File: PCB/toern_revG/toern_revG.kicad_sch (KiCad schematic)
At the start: 96 parts, among them IC1 BQ24075TRGTR, J1 AudioJack3_Switch, J10 Conn_01x02, J11 Conn_01x05, J11.5 Conn_01x05, J12 Conn_01x05, J13 Conn_01x05, J14 Conn_01x05, J15 Conn_01x05, J16 BATTERY, J17 AudioJack3_Ground, J3 AudioJack3_Ground, J4 USB_C_Receptacle_USB2.0, J5 AudioJack3_Switch, J6 AudioJack3_Switch, J7 AudioJack3_Switch, J8 Micro_SD_Card, J9 Conn_01x03, U1 SPX3819M5-L-3-3, U10 01x05 Connector_PinSocket_2.5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, U11 01x05 Connector_PinSocket_2.5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, U12 01x05 Connector_PinSocket_2.5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, U13 PAM8403D, U2 SPX3819M5-L-1-8, U3 SGTL5000XNBA3, U4 TLP2361V4_E, U5 74LVC2G14, U6 Teensy4.1, U7 SPX3819M5-L-3-3, U9 01x05 Connector_PinSocket_2.5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

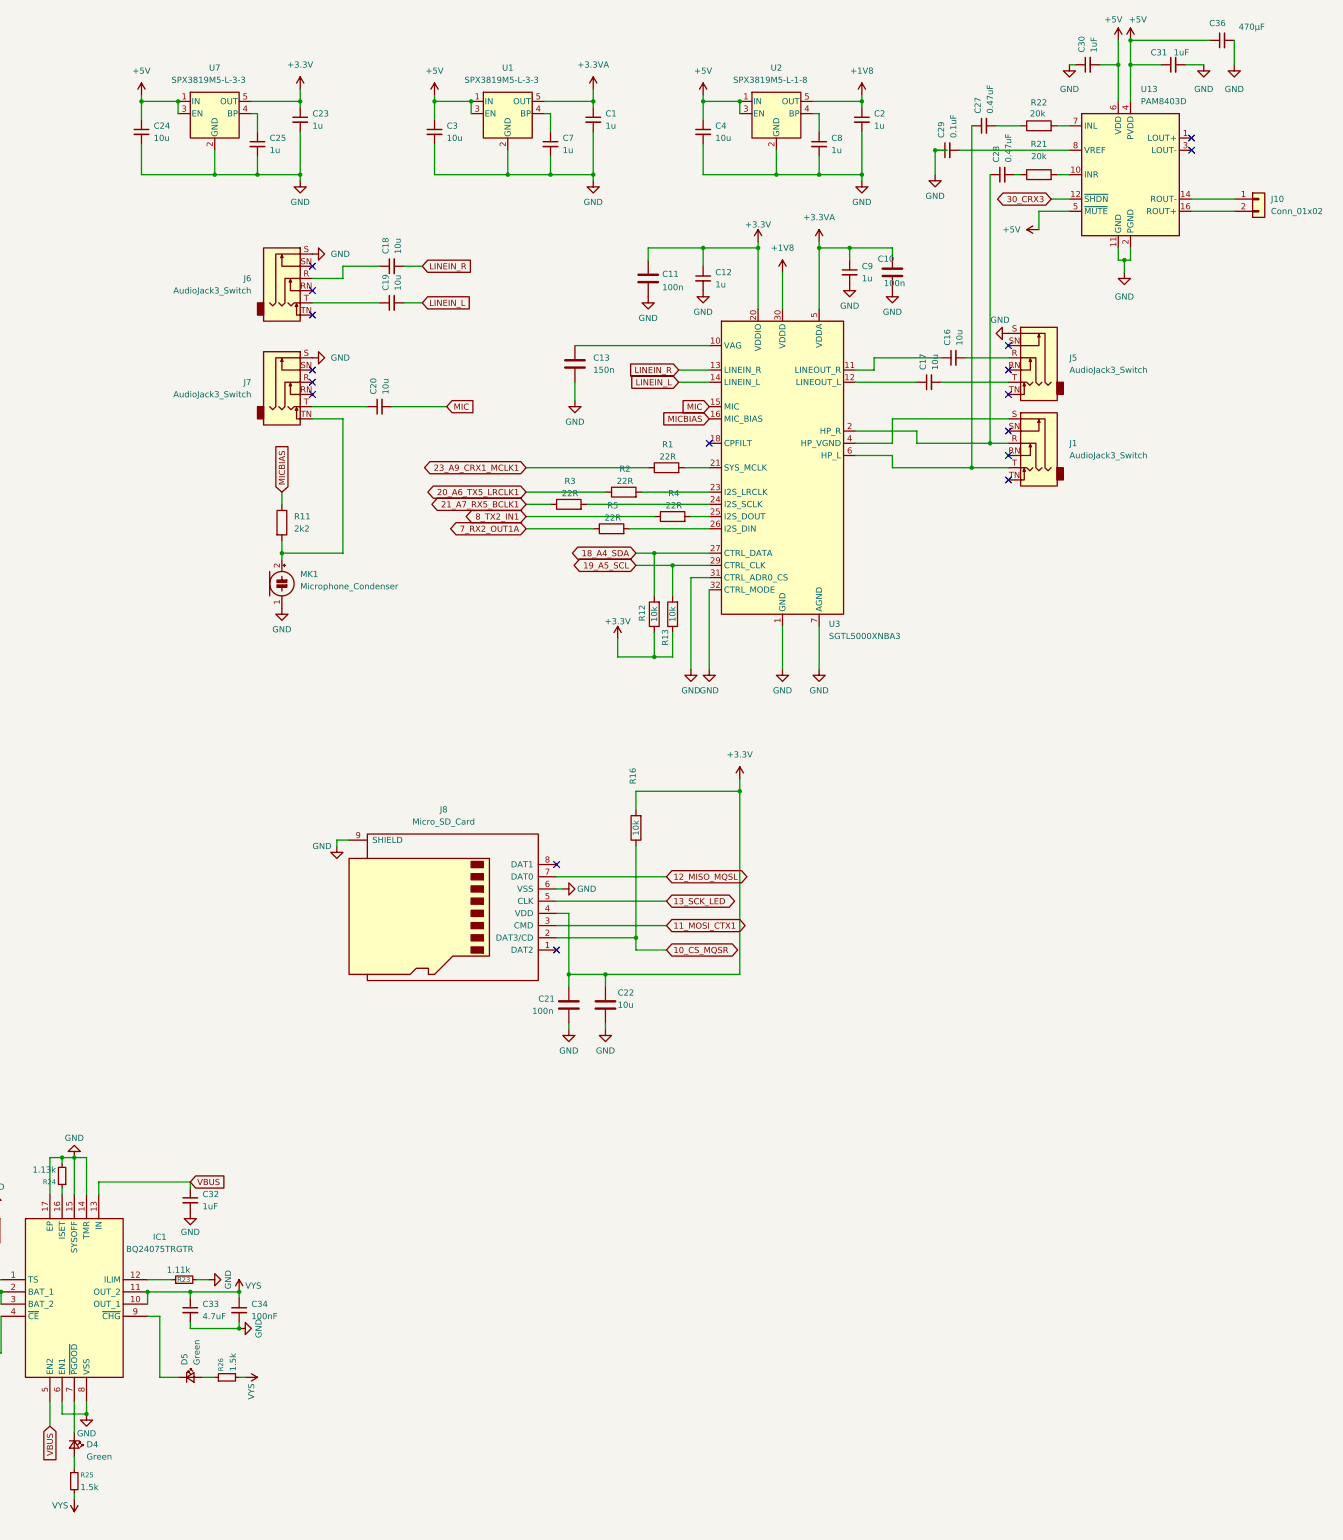
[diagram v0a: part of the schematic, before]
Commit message: fixes for HD Displays 32x16
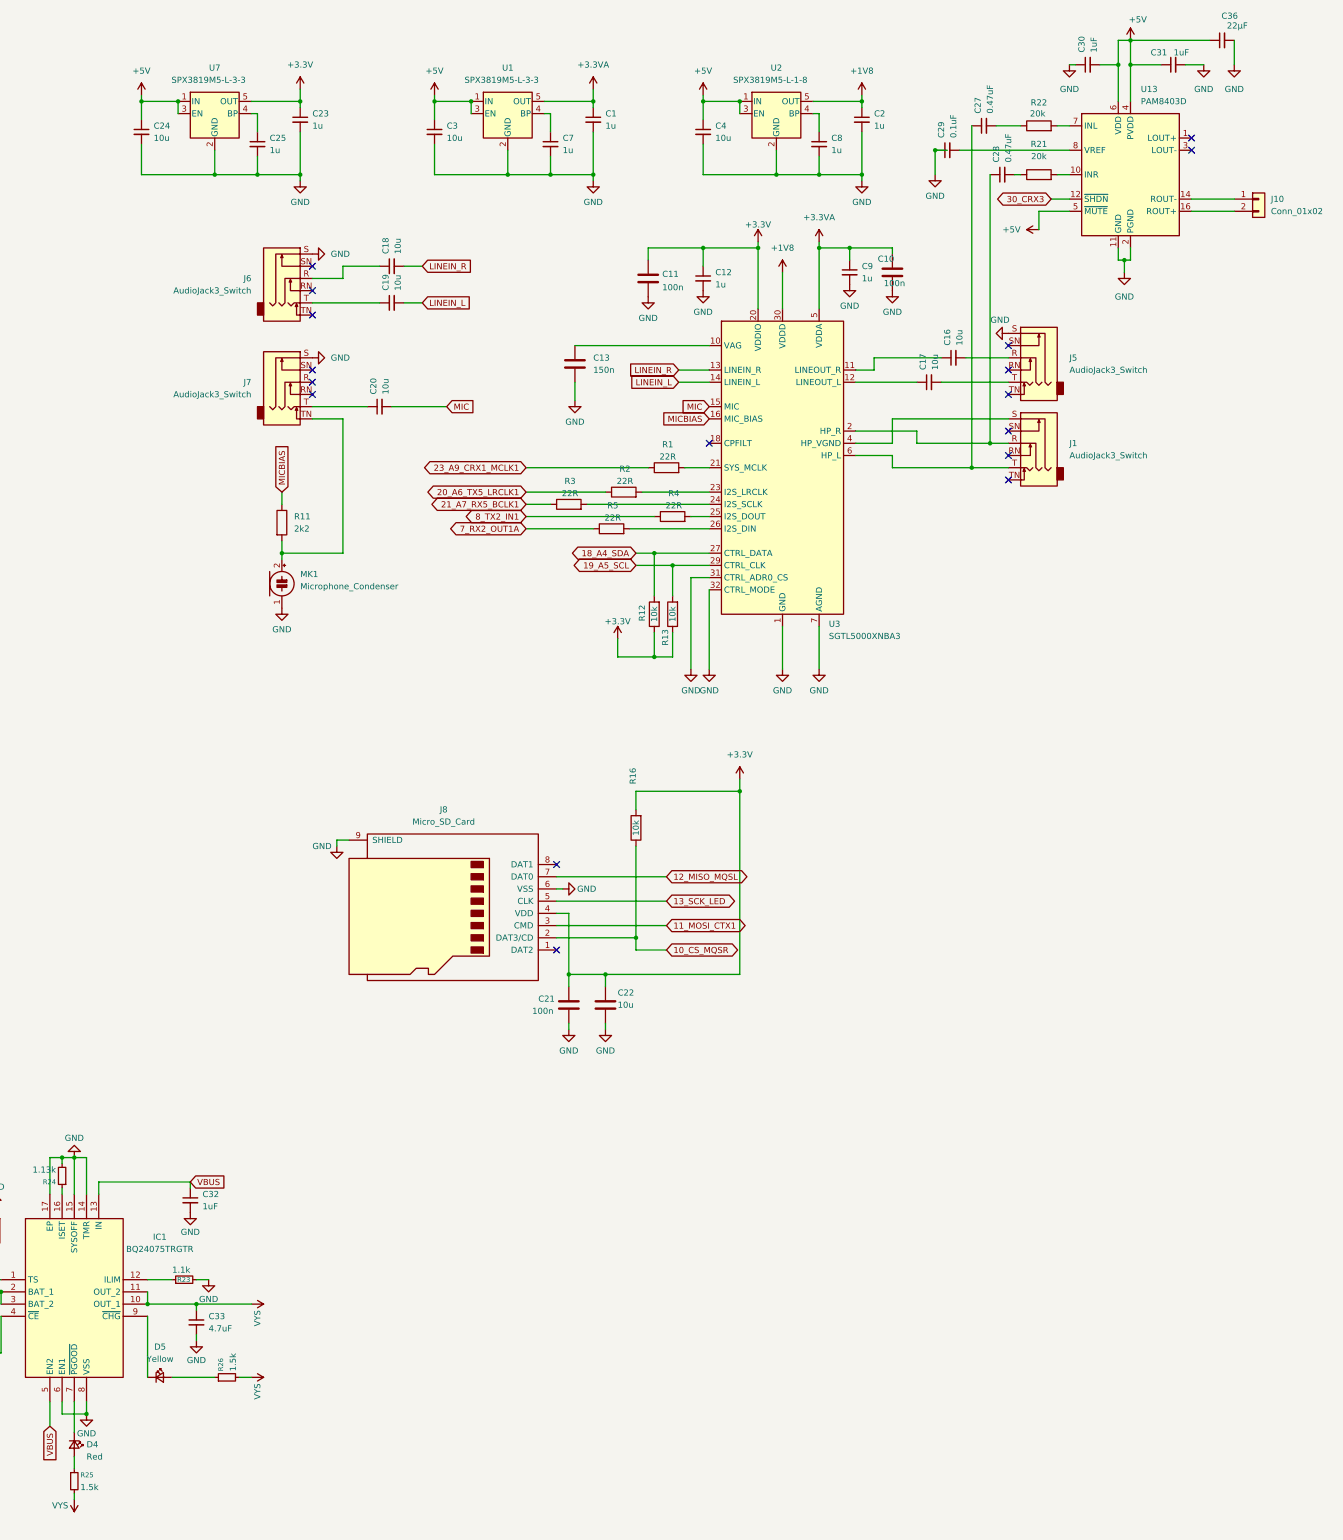
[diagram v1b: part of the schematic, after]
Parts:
- removed C34: 100nF, Capacitor_SMD:C_0402_1005Metric, symbol Device:C_Small
- C32: lcsc# (none) -> C15849
- C35: lscs# (none) -> C1705
- C36: value 470µF -> 22µF; lcsc# (none) -> C1859
- D4: value Green -> Red; lcsc# (none) -> C71911
- D5: value Green -> Yellow; lcsc# (none) -> C74342
- R14: lcsc# C98220 -> C25744
- R23: value 1.11k -> 1.1k; lcsc# (none) -> C25860
- R24: lcsc# (none) -> C67014
- R25, R26: lcsc# (none) -> C25867
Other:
- moved on the sheet: C33, D5

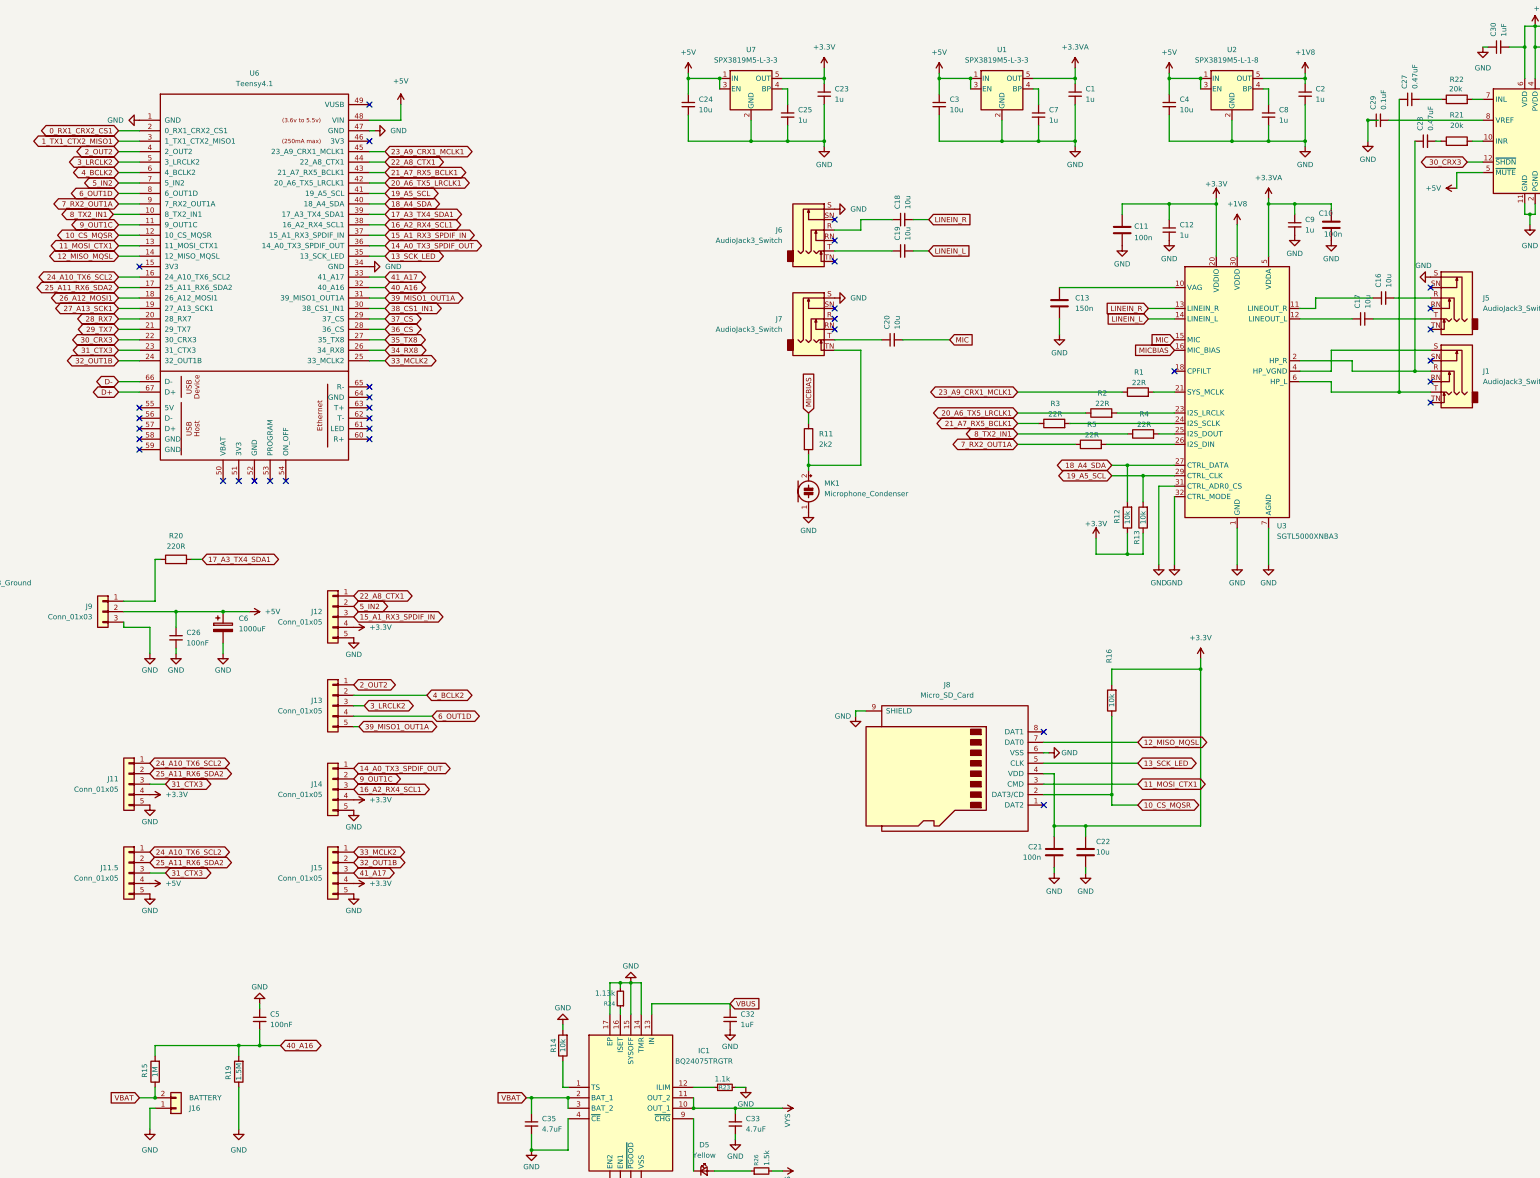
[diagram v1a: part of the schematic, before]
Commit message: extended reverb and muteAll fix for Draw==R
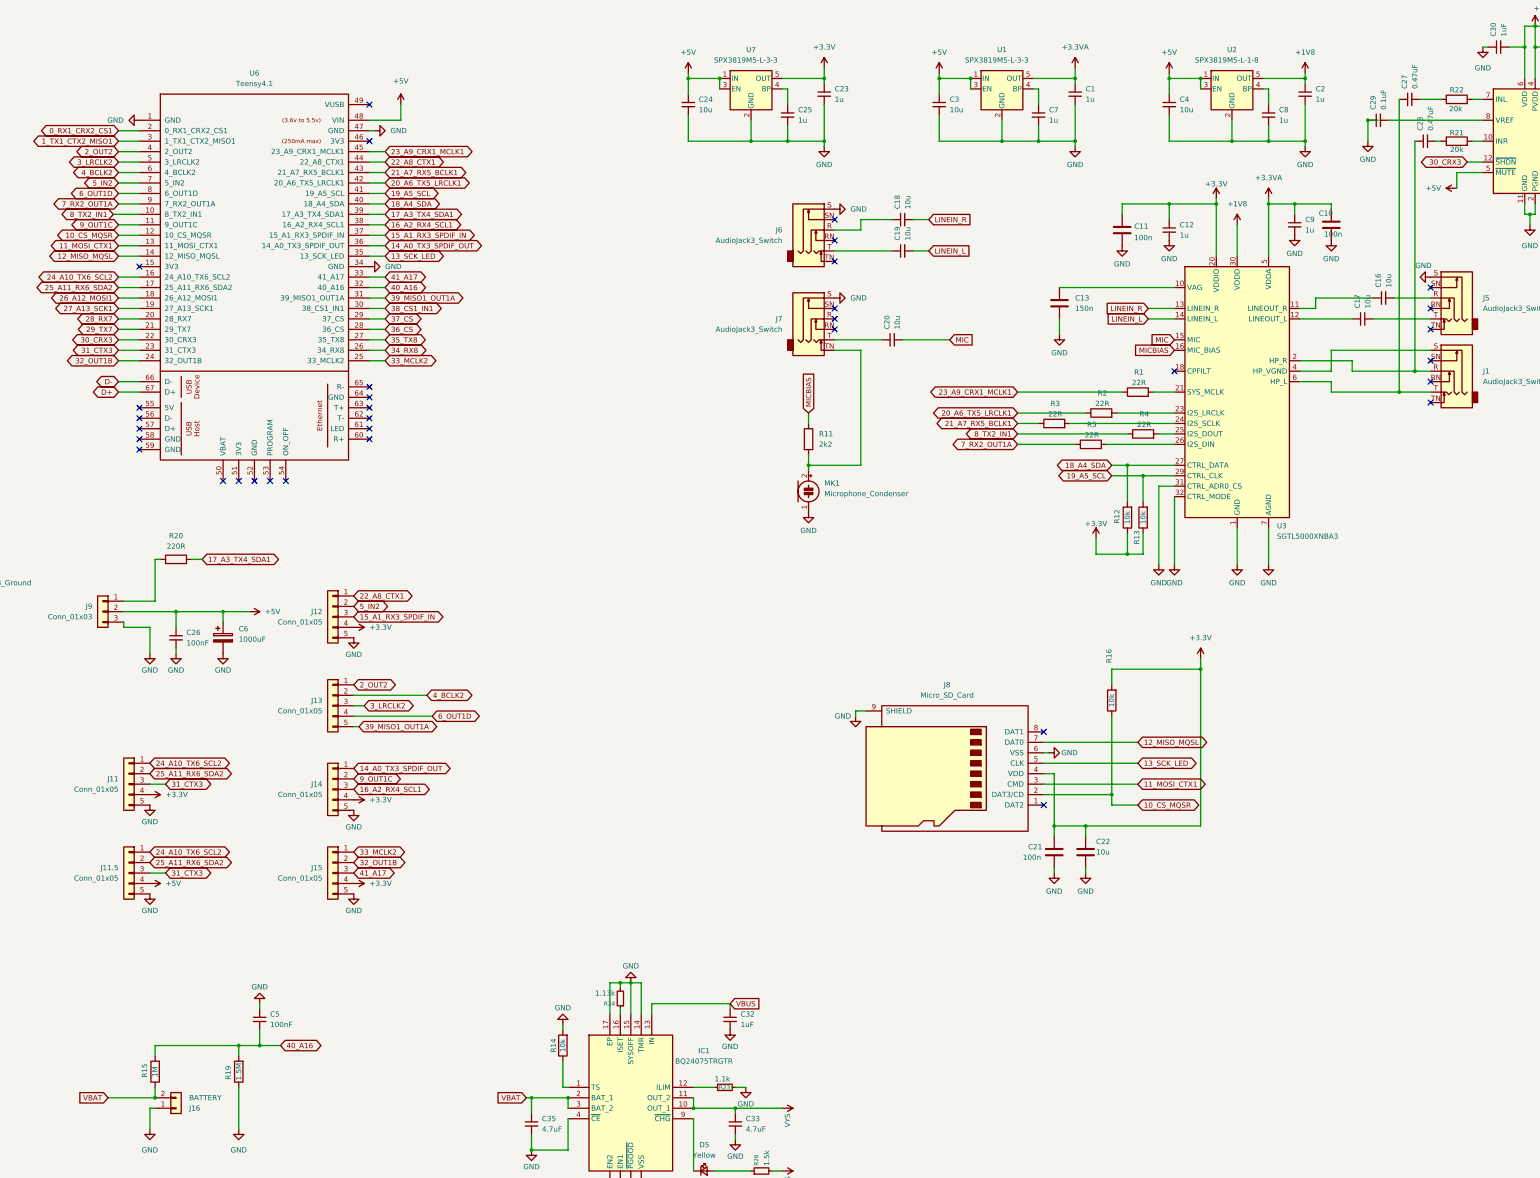
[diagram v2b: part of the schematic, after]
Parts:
- C26: lcsc# (none) -> C1525
- C35: lcsc# (none) -> C1705
- C6: lcsc# (none) -> C5686929
- IC1: lcsc# (none) -> C544783
- J17, J3: lcsc# (none) -> C4992548
- MK1: footprint Sensor_Audio:POM-2244P-C3310-2-R -> GMI6027P-2C38DB-RF75; lcsc# C3273559 -> C529951
- R21, R22: lcsc# (none) -> C4328; lcsnr# C4184 -> C4328
- S1: lcsc# (none) -> C3664594
- U13: lcsc# (none) -> C17337
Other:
- moved on the sheet: C6

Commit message: fixed PCB and shematics for RevG
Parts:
- added MountingHole1, MountingHole2, MountingHole3: MountingHole_2.2mm_M2, MountingHole:MountingHole_2.2mm_M2, symbol Mechanical:MountingHole
- C26: footprint Capacitor_SMD:C_0201_0603Metric -> Capacitor_SMD:C_0603_1608Metric; lcsc# C1525 -> C1590
- C29: value 0.1uF -> 100nF; lcsc# C1525 -> C1590
- C30, C31: lcsc# C1848 -> C15849
- C35: lscs# C1705 -> (none)
- C36: lcsc# C1859 -> C59461
- C5: footprint Capacitor_SMD:C_0402_1005Metric -> Capacitor_SMD:C_0603_1608Metric; LCSC (none) -> C1590; lcsc# C1525 -> C1590
- IC1: LCSC (none) -> C544783
- J16: value BATTERY -> Conn_01x02
- J17, J3: LCSC (none) -> C4992548
- MK1: footprint GMI6027P-2C38DB-RF75 -> Sensor_Audio:POM-2244P-C3310-2-R
- R11: value 2k2 -> 2.2k
- R12, R13, R16: lcsc# C98220 -> C25744
- R21, R22: LCSC (none) -> C4328; lcsnr# C4328 -> (none)
- S1: footprint EG2219 -> Button_Switch_THT:SW_E-Switch_EG2219_DPDT_Angled; LCSC (none) -> C3664594
- U13: LCSC (none) -> C17337
- U3: LCSC (none) -> C5196742; lcsc# C5196742 -> C5196742
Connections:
- net +5V: now also J9.3 (Pin_3); no longer J9.2 (Pin_2)
- net GND: now also J9.2 (Pin_2); no longer J9.3 (Pin_3)
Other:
- moved on the sheet: C26, C6, J9, R20

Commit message: fixed PCB and shematics for RevG 2
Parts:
- added J18, J19, J2, J20, J21, J22, J23, J24: Conn_01x05_Socket, Connector_PinSocket_2.54mm:PinSocket_1x05_P2.54mm_Vertical, symbol Connector:Conn_01x05_Socket
- U10, U11, U12, U9: now left out of the parts list
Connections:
- net +5V: now also J18.2 (Pin_2), J19.2 (Pin_2), J2.2 (Pin_2), J20.2 (Pin_2), J21.2 (Pin_2), J22.2 (Pin_2), J23.2 (Pin_2), J24.2 (Pin_2)
- net 18_A4_SDA: now also J18.3 (Pin_3), J19.3 (Pin_3), J2.3 (Pin_3), J20.3 (Pin_3), J21.3 (Pin_3), J22.3 (Pin_3), J23.3 (Pin_3), J24.3 (Pin_3)
- net 19_A5_SCL: now also J18.4 (Pin_4), J19.4 (Pin_4), J2.4 (Pin_4), J20.4 (Pin_4), J21.4 (Pin_4), J22.4 (Pin_4), J23.4 (Pin_4), J24.4 (Pin_4)
- net 27_A13_SCK1: now also J18.5 (Pin_5), J19.5 (Pin_5), J2.5 (Pin_5), J20.5 (Pin_5), J21.5 (Pin_5), J22.5 (Pin_5), J23.5 (Pin_5), J24.5 (Pin_5)
- net GND: now also J18.1 (Pin_1), J19.1 (Pin_1), J2.1 (Pin_1), J20.1 (Pin_1), J21.1 (Pin_1), J22.1 (Pin_1), J23.1 (Pin_1), J24.1 (Pin_1)
